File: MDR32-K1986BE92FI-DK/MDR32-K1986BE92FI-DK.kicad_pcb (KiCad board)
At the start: 2 copper layers, 69.6 x 21.4 mm, 57 parts, among them J1 Conn_PROBE, J2 PIN_A, J3 SYS_A, J4 USB_C_Receptacle_USB2.0_16P, J5 PIN_B, J6 SYS_B, Q1 AO3401A, SW1 IT-1181, SW2 SW_DIP_x02, SW3 IT-1181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

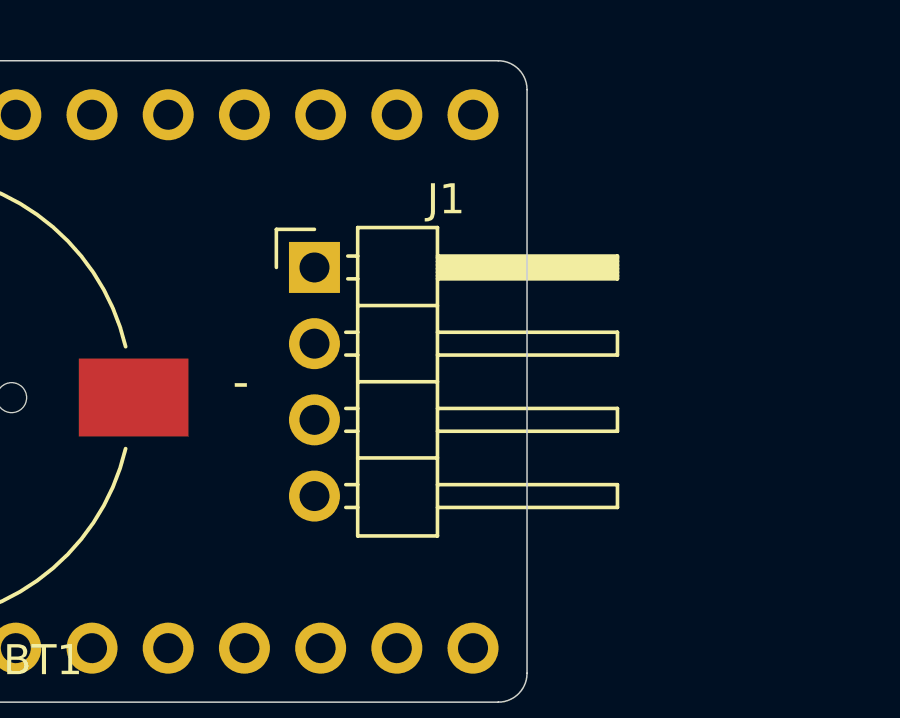
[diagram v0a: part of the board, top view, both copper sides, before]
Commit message: fix sw pin header
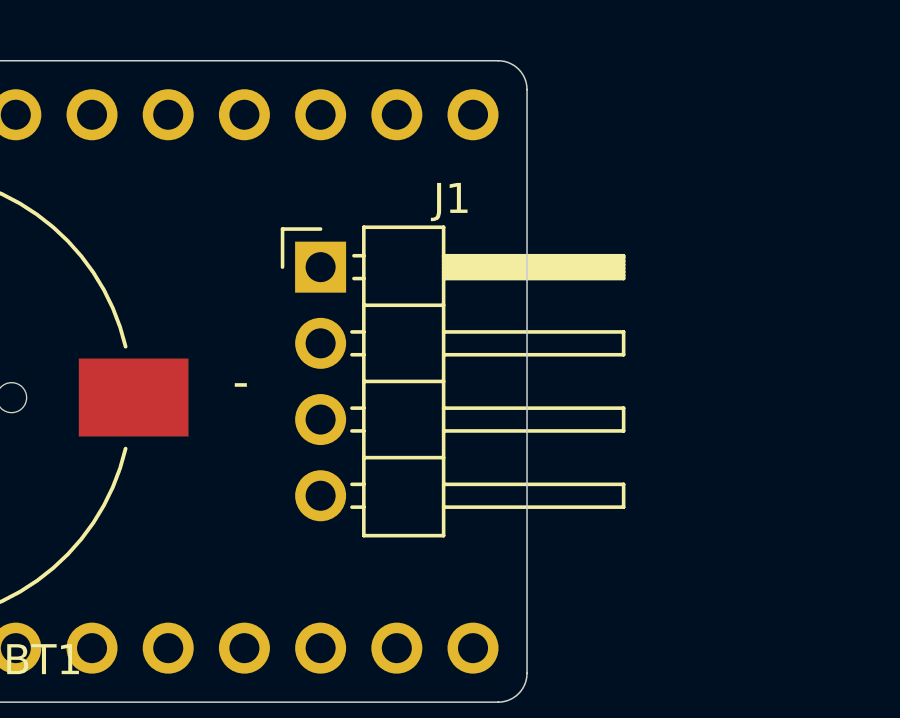
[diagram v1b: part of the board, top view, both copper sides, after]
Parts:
- moved J1 0.21 mm to (79.8, 23.9)
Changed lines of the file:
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@@
 		(tags "resistor")
 		(property "Reference" "R20"
-			(at 0 -1.17 360)
+			(at 0 -1.17 0)
 			(layer "F.SilkS")
 			(effects
@@
 		)
 		(property "Value" "470"
-			(at 0 1.17 360)
+			(at 0 1.17 0)
 			(layer "F.Fab")
 			(effects
@@
 		)
 		(fp_text user "${REFERENCE}"
-			(at 0 0 360)
+			(at 0 0 0)
 			(layer "F.Fab")
 			(effects
@@
 		(at 66 28.27 180)
 		(property "Reference" "BT1"
-			(at -4.544 -8.754 360)
+			(at -4.544 -8.754 0)
 			(layer "F.SilkS")
 			(effects
@@
 		)
 		(property "Value" "CR1220"
-			(at 1.071 8.538 360)
+			(at 1.071 8.538 0)
 			(layer "F.Fab")
 			(effects
@@
 		)
 		(property "Footprint" "MDR32-K1986BE92FI-DK:MPD_BC501SM-TR"
-			(at 0 0 360)
+			(at 0 0 0)
 			(layer "F.Fab")
 			(hide yes)
@@
 		)
 		(property "Datasheet" ""
-			(at 0 0 360)
+			(at 0 0 0)
 			(layer "F.Fab")
 			(hide yes)
@@
 		)
 		(property "Description" "Single-cell battery"
-			(at 0 0 360)
+			(at 0 0 0)
 			(layer "F.Fab")
 			(hide yes)
@@
 		)
 		(fp_text user "-"
-			(at -11.14 0.52 360)
+			(at -11.14 0.52 0)
 			(layer "F.SilkS")
 			(effects
@@
 		)
 		(fp_text user "+"
-			(at 10.49 0.57 360)
+			(at 10.49 0.57 0)
 			(layer "F.SilkS")
 			(effects
@@
 		(locked yes)
 		(layer "F.Cu")
-		(at 79.595 23.93)
+		(at 79.8 23.92)
 		(descr "Through hole angled pin header, 1x04, 2.54mm pitch, 6mm pin length, single row")
 		(tags "Through hole angled pin header THT 1x04 2.54mm single row")
@@
 		)
 		(fp_text user "${REFERENCE}"
-			(at 1.925 0 360)
+			(at 1.925 0 0)
 			(layer "F.Fab")
 			(effects
@@
 		(tags "capacitor")
 		(property "Reference" "C1"
-			(at 0 1.68 360)
+			(at 0 1.68 0)
 			(layer "B.SilkS")
 			(effects
@@
 		)
 		(property "Value" "10µF"
-			(at 0 -1.68 360)
+			(at 0 -1.68 0)
 			(layer "B.Fab")
 			(effects
@@
 		)
 		(fp_text user "${REFERENCE}"
-			(at 0 0 360)
+			(at 0 0 0)
 			(layer "B.Fab")
 			(effects
@@
 		(tags "CMS SOT")
 		(property "Reference" "U1"
-			(at 0 4.5 360)
+			(at 0 4.5 0)
 			(layer "B.SilkS")
 			(effects
@@
 		)
 		(property "Value" "LM1117GS-3.3"
-			(at 0 -4.5 360)
+			(at 0 -4.5 0)
 			(layer "B.Fab")
 			(effects
@@
 		(tags "capacitor")
 		(property "Reference" "C2"
-			(at 0 1.68 360)
+			(at 0 1.68 0)
 			(layer "B.SilkS")
 			(effects
@@
 		)
 		(property "Value" "10µF"
-			(at 0 -1.68 360)
+			(at 0 -1.68 0)
 			(layer "B.Fab")
 			(effects
@@
 		)
 		(fp_text user "${REFERENCE}"
-			(at 0 0 360)
+			(at 0 0 0)
 			(layer "B.Fab")
 			(effects
@@
 		(tags "SOD-123")
 		(property "Reference" "D1"
-			(at 0 2 360)
+			(at 0 2 0)
 			(layer "B.SilkS")
 			(effects
@@
 		)
 		(property "Value" "B5819W"
-			(at 0 -2.1 360)
+			(at 0 -2.1 0)
 			(layer "B.Fab")
 			(effects
@@
 		)
 		(fp_text user "${REFERENCE}"
-			(at 0 2 360)
+			(at 0 2 0)
 			(layer "B.Fab")
 			(effects

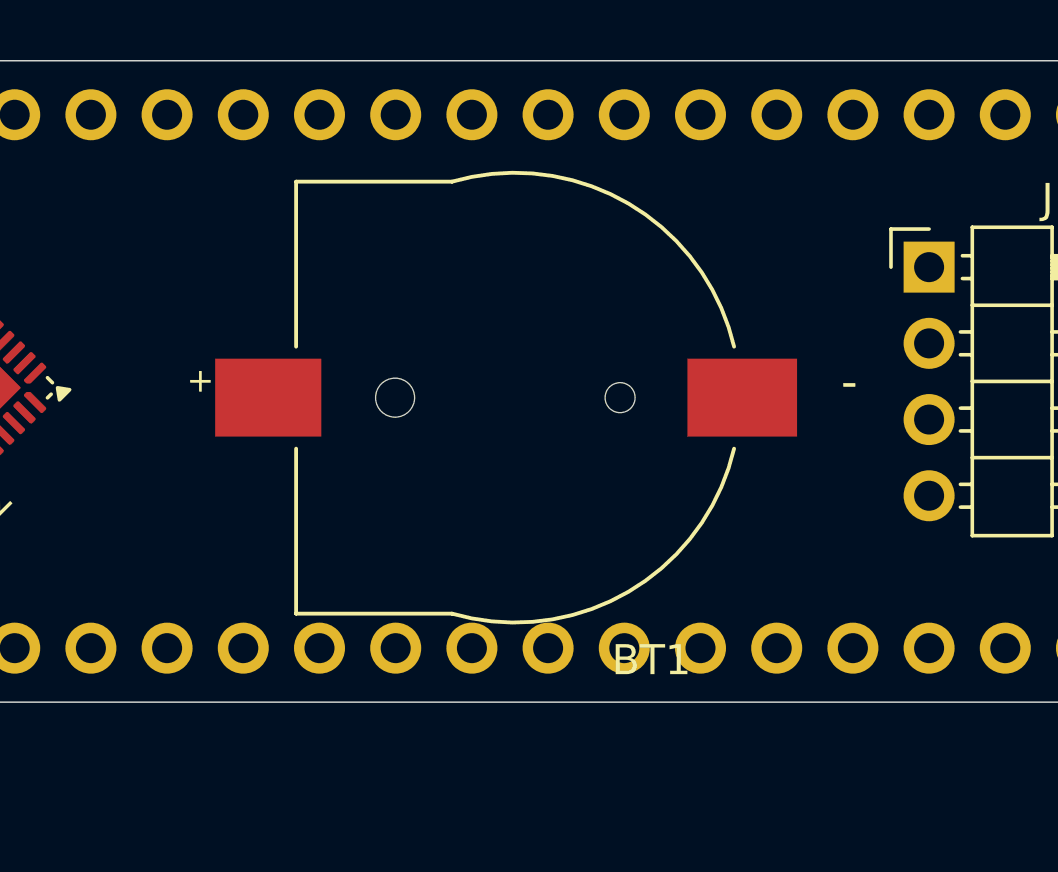
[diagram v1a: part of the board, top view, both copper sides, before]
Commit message: exclude battery holder
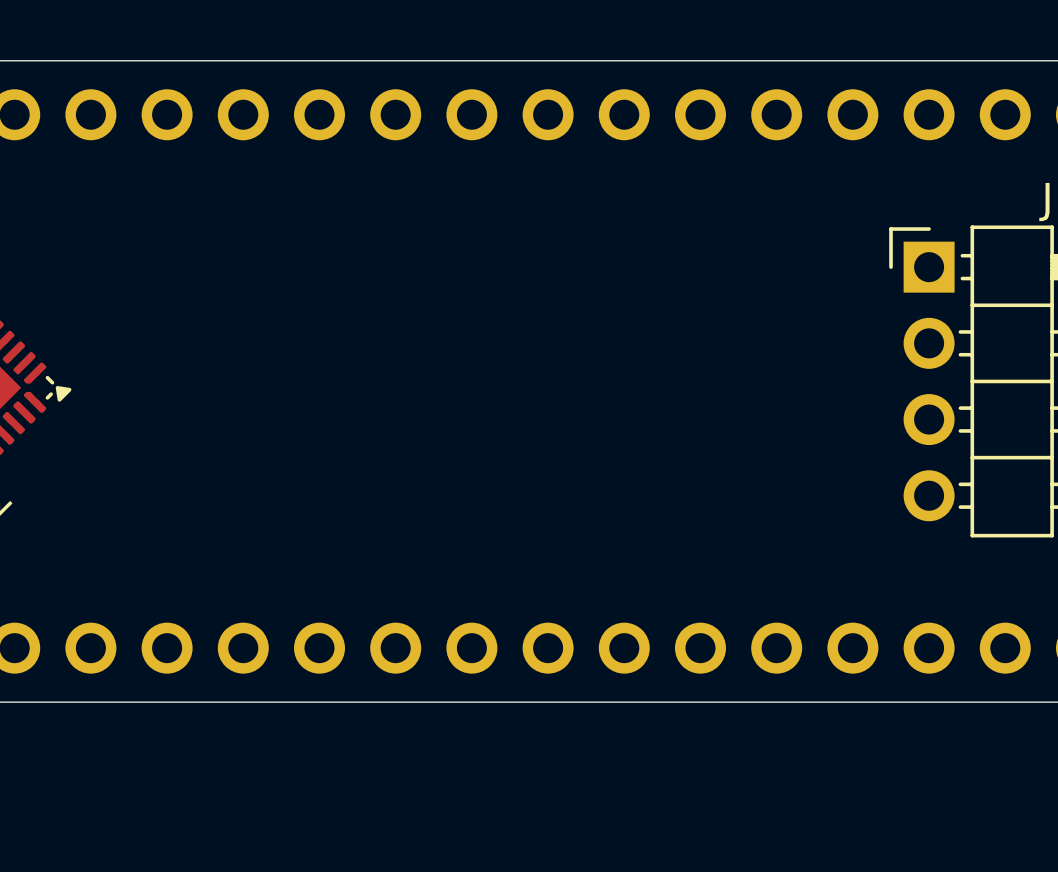
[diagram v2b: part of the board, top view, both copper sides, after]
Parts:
- removed BT1: CR1220, MDR32-K1986BE92FI-DK:MPD_BC501SM-TR
- C11: value 12pF -> 0.1µF
- C12: value 0.1µF -> 12pF
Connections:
- C11 pad 1: /OSC_OUT -> +BATT
- C12 pad 1: +BATT -> /OSC_OUT
- J2 pad 2: GND -> +BATT_SRC
- J3 pad 3: +BATT_SRC -> GND

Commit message: update cap sizes
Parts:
- C10, C11, C12, C4, C5, C6, C7, C8, C9: footprint Capacitor_SMD:C_0402_1005Metric -> Capacitor_SMD:C_0603_1608Metric

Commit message: update resistors sizes
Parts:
- R1, R10, R11, R12, R13, R14, R15, R16, R17, R18, R19, R2, R20, R21, R22, R3, R4, R5, R6, R7, R8, R9: footprint Resistor_SMD:R_0402_1005Metric -> Resistor_SMD:R_0603_1608Metric

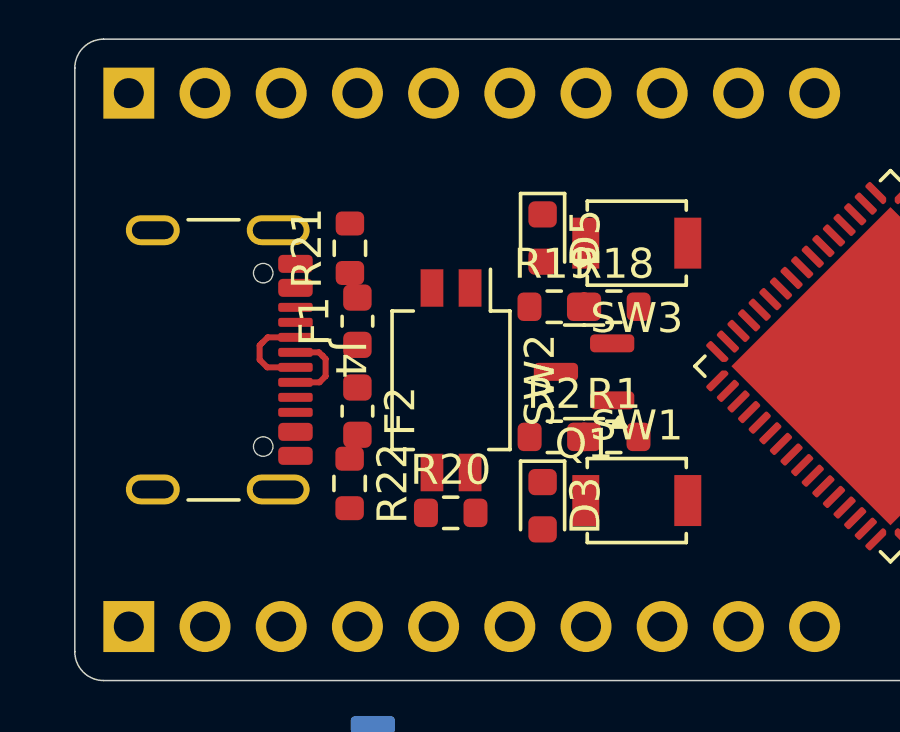
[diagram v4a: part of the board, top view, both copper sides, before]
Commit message: update LED sizes
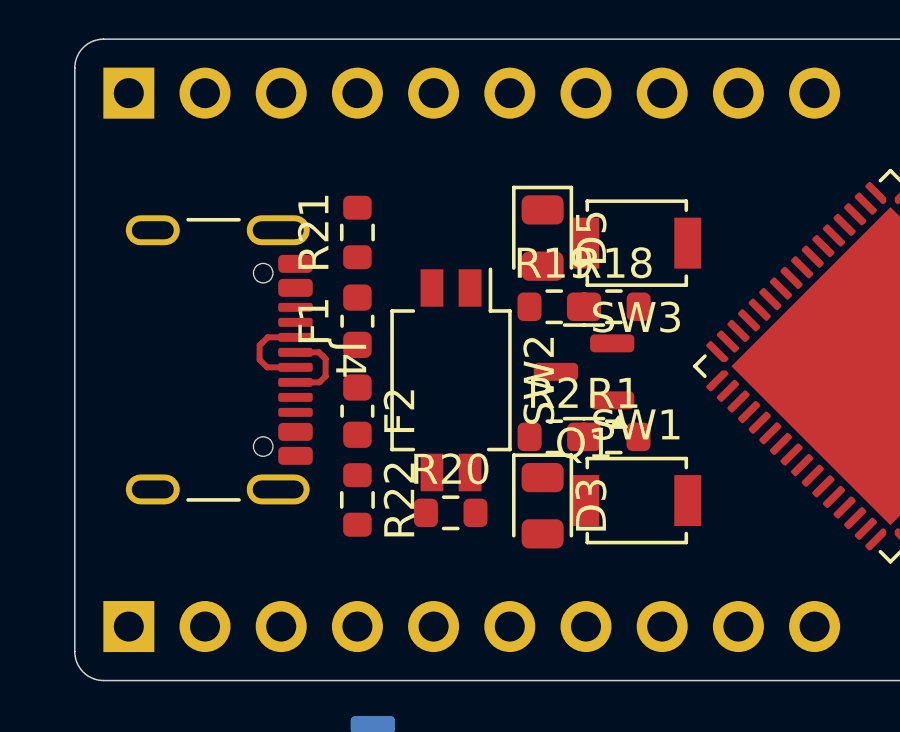
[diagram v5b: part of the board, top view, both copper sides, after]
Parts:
- D3, D5: footprint LED_SMD:LED_0603_1608Metric -> LED_SMD:LED_0805_2012Metric
- moved R22 0.61 mm to (26.5, 32.4)
- moved R21 0.58 mm to (26.5, 23.5)
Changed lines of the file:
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@@
 	(net 68 "unconnected-(J4-SBU1-PadA8)")
 	(net 69 "unconnected-(J4-SBU2-PadB8)")
-	(footprint "LED_SMD:LED_0603_1608Metric"
+	(footprint "LED_SMD:LED_0805_2012Metric"
 		(layer "F.Cu")
 		(at 32.6325 23.67 -90)
-		(descr "LED SMD 0603 (1608 Metric), square (rectangular) end terminal, IPC_7351 nominal, (Body size source: http://www.tortai-tech.com/upload/download/2011102023233369053.pdf), generated with kicad-footprint-generator")
+		(descr "LED SMD 0805 (2012 Metric), square (rectangular) end terminal, IPC_7351 nominal, (Body size source: https://docs.google.com/spreadsheets/d/1BsfQQcO9C6DZCsRaXUlFlo91Tg2WpOkGARC1WS5S8t0/edit?usp=sharing), generated with kicad-footprint-generator")
 		(tags "LED")
 		(property "Reference" "D5"
-			(at 0 -1.43 90)
+			(at 0 -1.65 -90)
 			(layer "F.SilkS")
 			(effects
@@
 		)
 		(property "Value" "LED"
-			(at 0 1.43 90)
+			(at 0 1.65 -90)
 			(layer "F.Fab")
 			(effects
@@
 			)
 		)
-		(property "Footprint" "LED_SMD:LED_0603_1608Metric"
+		(property "Footprint" "LED_SMD:LED_0805_2012Metric"
 			(at 0 0 -90)
 			(unlocked yes)
@@
 		(attr smd)
 		(fp_line
-			(start -1.485 0.735)
-			(end 0.8 0.735)
+			(start -1.685 0.96)
+			(end 1 0.96)
 			(stroke
 				(width 0.12)
@@
 		)
 		(fp_line
-			(start -1.485 -0.735)
-			(end -1.485 0.735)
+			(start -1.685 -0.96)
+			(end -1.685 0.96)
 			(stroke
 				(width 0.12)
@@
 		)
 		(fp_line
-			(start 0.8 -0.735)
-			(end -1.485 -0.735)
+			(start 1 -0.96)
+			(end -1.685 -0.96)
 			(stroke
 				(width 0.12)
@@
 		)
 		(fp_line
-			(start -1.48 0.73)
-			(end -1.48 -0.73)
+			(start -1.68 0.95)
+			(end -1.68 -0.95)
 			(stroke
 				(width 0.05)
@@
 		)
 		(fp_line
-			(start 1.48 0.73)
-			(end -1.48 0.73)
+			(start 1.68 0.95)
+			(end -1.68 0.95)
 			(stroke
 				(width 0.05)
@@
 		)
 		(fp_line
-			(start -1.48 -0.73)
-			(end 1.48 -0.73)
+			(start -1.68 -0.95)
+			(end 1.68 -0.95)
 			(stroke
 				(width 0.05)
@@
 		)
 		(fp_line
-			(start 1.48 -0.73)
-			(end 1.48 0.73)
+			(start 1.68 -0.95)
+			(end 1.68 0.95)
 			(stroke
 				(width 0.05)
@@
 		)
 		(fp_line
-			(start -0.8 0.4)
-			(end 0.8 0.4)
+			(start -1 0.6)
+			(end 1 0.6)
 			(stroke
 				(width 0.1)
@@
 		)
 		(fp_line
-			(start 0.8 0.4)
-			(end 0.8 -0.4)
+			(start 1 0.6)
+			(end 1 -0.6)
 			(stroke
 				(width 0.1)
@@
 		)
 		(fp_line
-			(start -0.8 -0.1)
-			(end -0.8 0.4)
+			(start -1 -0.3)
+			(end -1 0.6)
 			(stroke
 				(width 0.1)
@@
 		)
 		(fp_line
-			(start -0.5 -0.4)
-			(end -0.8 -0.1)
+			(start -0.7 -0.6)
+			(end -1 -0.3)
 			(stroke
 				(width 0.1)
@@
 		)
 		(fp_line
-			(start 0.8 -0.4)
-			(end -0.5 -0.4)
+			(start 1 -0.6)
+			(end -0.7 -0.6)
 			(stroke
 				(width 0.1)
@@
 		)
 		(fp_text user "${REFERENCE}"
-			(at 0 0 90)
+			(at 0 0 -90)
 			(layer "F.Fab")
 			(effects
 				(font
-					(size 0.4 0.4)
-					(thickness 0.06)
+					(size 0.5 0.5)
+					(thickness 0.08)
 				)
 			)
 		)
 		(pad "1" smd roundrect
-			(at -0.7875 0 270)
-			(size 0.875 0.95)
+			(at -0.9375 0 270)
+			(size 0.975 1.4)
 			(layers "F.Cu" "F.Paste" "F.Mask")
 			(roundrect_rratio 0.25)
@@
 		)
 		(pad "2" smd roundrect
-			(at 0.7875 0 270)
-			(size 0.875 0.95)
+			(at 0.9375 0 270)
+			(size 0.975 1.4)
 			(layers "F.Cu" "F.Paste" "F.Mask")
 			(roundrect_rratio 0.25)
@@
 			(pintype "passive")
 		)
-		(model "${KICAD8_3DMODEL_DIR}/LED_SMD.3dshapes/LED_0603_1608Metric.wrl"
+		(model "${KICAD8_3DMODEL_DIR}/LED_SMD.3dshapes/LED_0805_2012Metric.wrl"
 			(offset
 				(xyz 0 0 0)
@@
 	(footprint "Resistor_SMD:R_0603_1608Metric"
 		(layer "F.Cu")
-		(at 26.2 31.85 -90)
+		(at 26.46 32.4 -90)
 		(descr "Resistor SMD 0603 (1608 Metric), square (rectangular) end terminal, IPC_7351 nominal, (Body size source: IPC-SM-782 page 72, https://www.pcb-3d.com/wordpress/wp-content/uploads/ipc-sm-782a_amendment_1_and_2.pdf), generated with kicad-footprint-generator")
 		(tags "resistor")
 		(property "Reference" "R22"
-			(at 0 -1.43 -90)
+			(at 0 -1.43 90)
 			(layer "F.SilkS")
 			(effects
@@
 		)
 		(property "Value" "5.1k"
-			(at 0 1.43 -90)
+			(at 0 1.43 90)
 			(layer "F.Fab")
 			(effects
@@
 		)
 		(fp_text user "${REFERENCE}"
-			(at 0 0 -90)
+			(at 0 0 90)
 			(layer "F.Fab")
 			(effects
@@
 	(footprint "Resistor_SMD:R_0603_1608Metric"
 		(layer "F.Cu")
-		(at 26.21 24.01 90)
+		(at 26.46 23.485 90)
 		(descr "Resistor SMD 0603 (1608 Metric), square (rectangular) end terminal, IPC_7351 nominal, (Body size source: IPC-SM-782 page 72, https://www.pcb-3d.com/wordpress/wp-content/uploads/ipc-sm-782a_amendment_1_and_2.pdf), generated with kicad-footprint-generator")
 		(tags "resistor")
@@
 		)
 	)
-	(footprint "LED_SMD:LED_0603_1608Metric"
+	(footprint "LED_SMD:LED_0805_2012Metric"
 		(layer "F.Cu")
 		(at 32.6325 32.5925 -90)
-		(descr "LED SMD 0603 (1608 Metric), square (rectangular) end terminal, IPC_7351 nominal, (Body size source: http://www.tortai-tech.com/upload/download/2011102023233369053.pdf), generated with kicad-footprint-generator")
+		(descr "LED SMD 0805 (2012 Metric), square (rectangular) end terminal, IPC_7351 nominal, (Body size source: https://docs.google.com/spreadsheets/d/1BsfQQcO9C6DZCsRaXUlFlo91Tg2WpOkGARC1WS5S8t0/edit?usp=sharing), generated with kicad-footprint-generator")
 		(tags "LED")
 		(property "Reference" "D3"
-			(at 0 -1.43 90)
+			(at 0 -1.65 -90)
 			(layer "F.SilkS")
 			(effects
@@
 		)
 		(property "Value" "LED"
-			(at 0 1.43 90)
+			(at 0 1.65 -90)
 			(layer "F.Fab")
 			(effects
@@
 			)
 		)
-		(property "Footprint" "LED_SMD:LED_0603_1608Metric"
+		(property "Footprint" "LED_SMD:LED_0805_2012Metric"
 			(at 0 0 -90)
 			(unlocked yes)
@@
 		(attr smd)
 		(fp_line
-			(start -1.485 0.735)
-			(end 0.8 0.735)
+			(start -1.685 0.96)
+			(end 1 0.96)
 			(stroke
 				(width 0.12)
@@
 		)
 		(fp_line
-			(start -1.485 -0.735)
-			(end -1.485 0.735)
+			(start -1.685 -0.96)
+			(end -1.685 0.96)
 			(stroke
 				(width 0.12)
@@
 		)
 		(fp_line
-			(start 0.8 -0.735)
-			(end -1.485 -0.735)
+			(start 1 -0.96)
+			(end -1.685 -0.96)
 			(stroke
 				(width 0.12)
@@
 		)
 		(fp_line
-			(start -1.48 0.73)
-			(end -1.48 -0.73)
+			(start -1.68 0.95)
+			(end -1.68 -0.95)
 			(stroke
 				(width 0.05)
@@
 		)
 		(fp_line
-			(start 1.48 0.73)
-			(end -1.48 0.73)
+			(start 1.68 0.95)
+			(end -1.68 0.95)
 			(stroke
 				(width 0.05)
@@
 		)
 		(fp_line
-			(start -1.48 -0.73)
-			(end 1.48 -0.73)
+			(start -1.68 -0.95)
+			(end 1.68 -0.95)
 			(stroke
 				(width 0.05)
@@
 		)
 		(fp_line
-			(start 1.48 -0.73)
-			(end 1.48 0.73)
+			(start 1.68 -0.95)
+			(end 1.68 0.95)
 			(stroke
 				(width 0.05)
@@
 		)
 		(fp_line
-			(start -0.8 0.4)
-			(end 0.8 0.4)
+			(start -1 0.6)
+			(end 1 0.6)
 			(stroke
 				(width 0.1)
@@
 		)
 		(fp_line
-			(start 0.8 0.4)
-			(end 0.8 -0.4)
+			(start 1 0.6)
+			(end 1 -0.6)
 			(stroke
 				(width 0.1)
@@
 		)
 		(fp_line
-			(start -0.8 -0.1)
-			(end -0.8 0.4)
+			(start -1 -0.3)
+			(end -1 0.6)
 			(stroke
 				(width 0.1)
@@
 		)
 		(fp_line
-			(start -0.5 -0.4)
-			(end -0.8 -0.1)
+			(start -0.7 -0.6)
+			(end -1 -0.3)
 			(stroke
 				(width 0.1)
@@
 		)
 		(fp_line
-			(start 0.8 -0.4)
-			(end -0.5 -0.4)
+			(start 1 -0.6)
+			(end -0.7 -0.6)
 			(stroke
 				(width 0.1)
@@
 		)
 		(fp_text user "${REFERENCE}"
-			(at 0 0 90)
+			(at 0 0 -90)
 			(layer "F.Fab")
 			(effects
 				(font
-					(size 0.4 0.4)
-					(thickness 0.06)
+					(size 0.5 0.5)
+					(thickness 0.08)
 				)
 			)
 		)
 		(pad "1" smd roundrect
-			(at -0.7875 0 270)
-			(size 0.875 0.95)
+			(at -0.9375 0 270)
+			(size 0.975 1.4)
 			(layers "F.Cu" "F.Paste" "F.Mask")
 			(roundrect_rratio 0.25)
@@
 		)
 		(pad "2" smd roundrect
-			(at 0.7875 0 270)
-			(size 0.875 0.95)
+			(at 0.9375 0 270)
+			(size 0.975 1.4)
 			(layers "F.Cu" "F.Paste" "F.Mask")
 			(roundrect_rratio 0.25)
@@
 			(pintype "passive")
 		)
-		(model "${KICAD8_3DMODEL_DIR}/LED_SMD.3dshapes/LED_0603_1608Metric.wrl"
+		(model "${KICAD8_3DMODEL_DIR}/LED_SMD.3dshapes/LED_0805_2012Metric.wrl"
 			(offset
 				(xyz 0 0 0)

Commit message: part position
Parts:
- moved C12 105.1 mm to (79.8, 45.1), turned to -90 degrees
- moved JP1 84.5 mm to (64.4, 49.7)
- moved JP2 84.5 mm to (64.4, 53.2)
- moved C11 74.4 mm to (43.6, 71.9)
- moved C8 69.5 mm to (43.6, 70.3)
- moved C3 69.5 mm to (44.0, 60.8)
- moved C5 69.5 mm to (43.6, 64.3)
- moved C6 69.5 mm to (43.6, 67.3)
- moved R7 67.3 mm to (39.2, 47.5)
- moved R6 66.4 mm to (39.2, 46.0)
- moved R5 65.4 mm to (39.2, 44.5)
- moved R4 64.5 mm to (39.2, 43.1)
- moved R3 63.6 mm to (39.2, 41.6)
- moved R14 60.5 mm to (42.8, 50.3)
- moved R13 59.6 mm to (42.8, 48.9)
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
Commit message: part position
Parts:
- moved R20 0.73 mm to (29.8, 32.4)
- moved SW2 0.73 mm to (29.8, 27.7)
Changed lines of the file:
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@@
 	(footprint "Resistor_SMD:R_0603_1608Metric"
 		(layer "F.Cu")
-		(at 29.57 33.09)
+		(at 29.845 32.41)
 		(descr "Resistor SMD 0603 (1608 Metric), square (rectangular) end terminal, IPC_7351 nominal, (Body size source: IPC-SM-782 page 72, https://www.pcb-3d.com/wordpress/wp-content/uploads/ipc-sm-782a_amendment_1_and_2.pdf), generated with kicad-footprint-generator")
 		(tags "resistor")
@@
 	(footprint "Button_Switch_SMD:SW_DIP_SPSTx02_Slide_Omron_A6H-2101_W6.15mm_P1.27mm"
 		(layer "F.Cu")
-		(at 29.58 28.41 -90)
+		(at 29.845 27.73 -90)
 		(descr "SMD 2x-dip-switch SPST Omron_A6H-2101, Slide, row spacing 6.15 mm (242 mils), body size  (see https://www.omron.com/ecb/products/pdf/en-a6h.pdf)")
 		(tags "SMD DIP Switch SPST Slide 6.15mm 242mil")
